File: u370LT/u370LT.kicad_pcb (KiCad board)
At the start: 2 copper layers, 1 part

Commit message: NB fixed up, SB started
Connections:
- U1 pad E16: unconnected-(U1-GTLREF-PadE16) -> Net-(U1-GTLREF-PadE16)
- U1 pad F17: unconnected-(U1-VTT-PadF17) -> Net-(U1-VTT-PadF17)
- U1 pad L4: Net-(U1-ST0) -> unconnected-(U1-ST0-PadL4)
- U1 pad M23: unconnected-(U1-GTLREF-PadM23) -> Net-(U1-GTLREF-PadE16)
- U1 pad M24: unconnected-(U1-VTT-PadM24) -> Net-(U1-VTT-PadF17)
- U1 pad M4: Net-(U1-ST0) -> unconnected-(U1-ST2-PadM4)

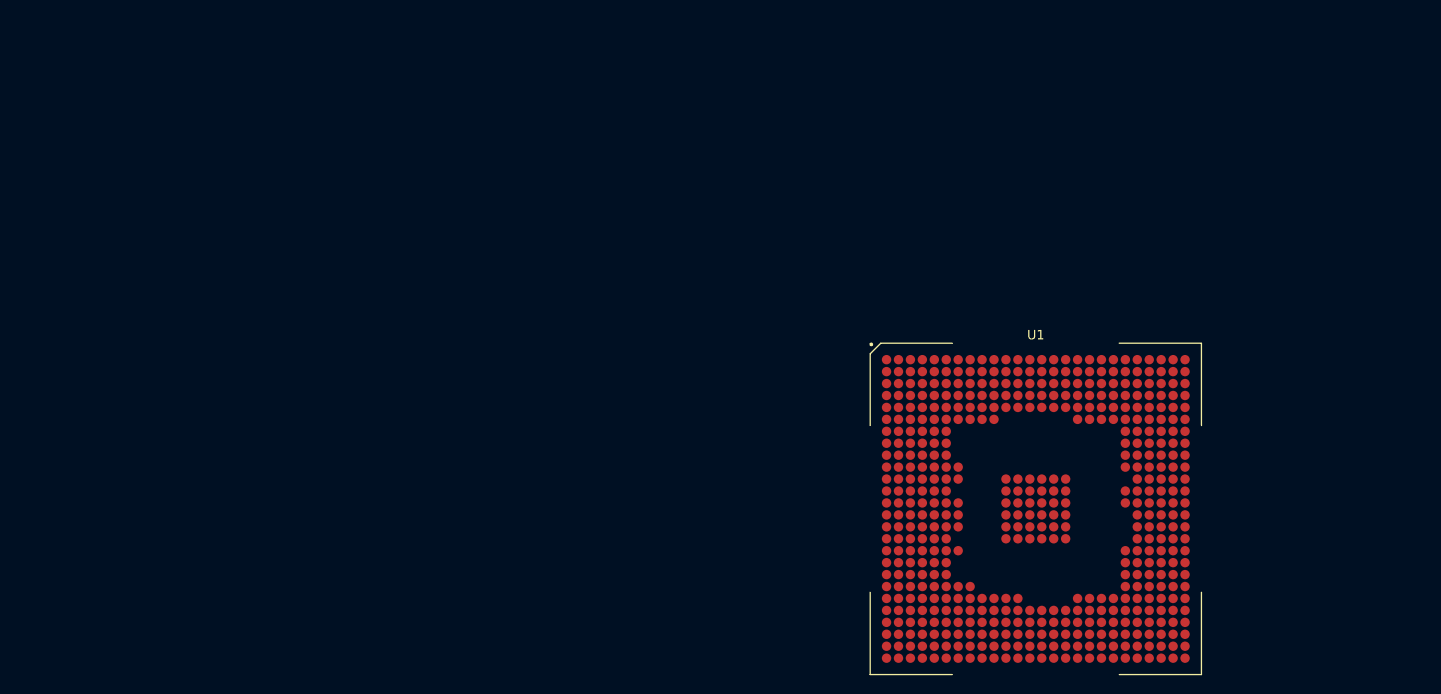
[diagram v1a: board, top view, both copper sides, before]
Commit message: Got NB/SB initially placed
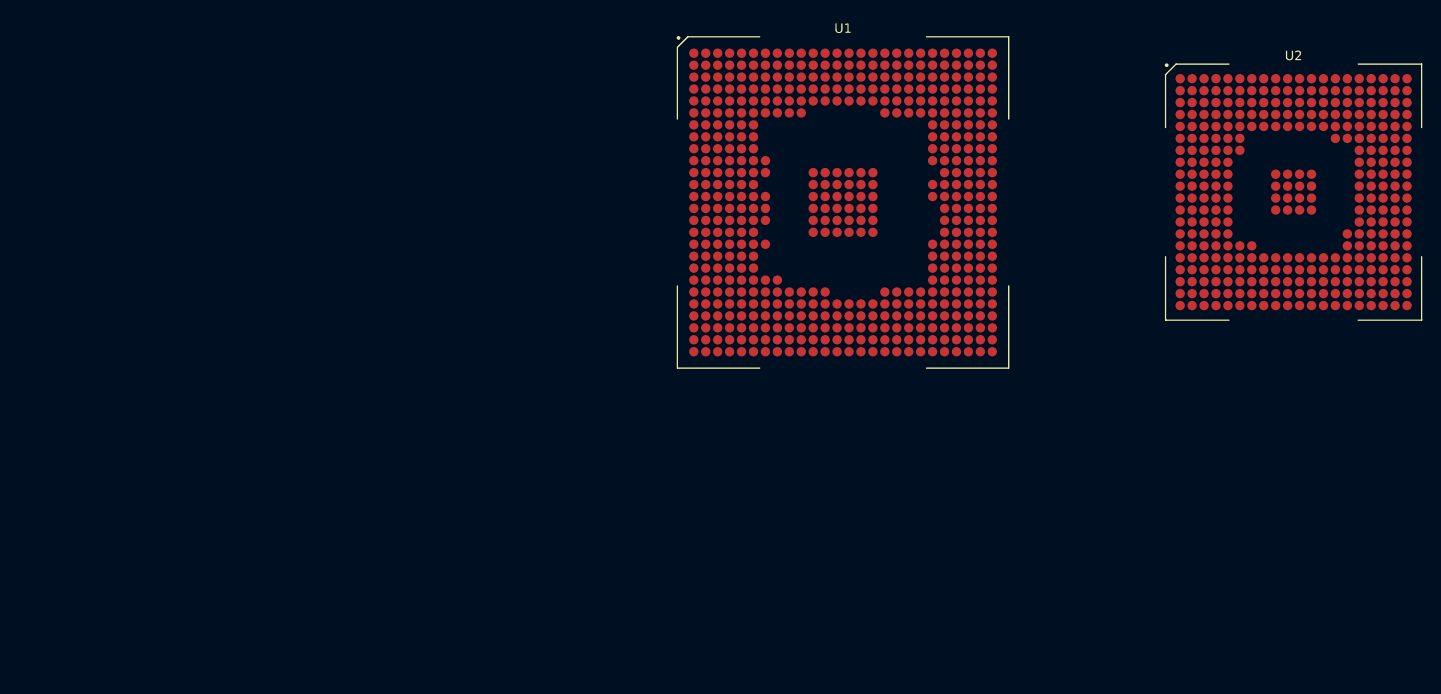
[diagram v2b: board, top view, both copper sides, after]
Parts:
- added U2: ~, Library:VT82C596B, F.Cu at (158.4, 47.0)
- U1: footprint Library:BGA-676_26x26_35.0x35.0mm -> Library:VT82C694X
- moved U1 38.5 mm to (110.5, 48.1)
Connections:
- U1 pad AF24: (no net) -> unconnected-(U1-CKE5-PadAF24)

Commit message: More 370 work
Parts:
- added U3: ~, Library:PGA370, F.Cu at (47.4, 51.2)
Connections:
- U1 pad A2: unconnected-(U1-AD20-PadA2) -> /North Bridge/AD20
- U1 pad A23: unconnected-(U1-HA29#-PadA23) -> HA29
- U1 pad A24: unconnected-(U1-HA24#-PadA24) -> HA24
- U1 pad A25: unconnected-(U1-HA22#-PadA25) -> HA22
- U1 pad A4: unconnected-(U1-AD25-PadA4) -> /North Bridge/AD25
- U1 pad A5: unconnected-(U1-AD29-PadA5) -> /North Bridge/AD29
- U1 pad B24: unconnected-(U1-HA27#-PadB24) -> HA27
- U1 pad B25: unconnected-(U1-HA20#-PadB25) -> HA20
- U1 pad B3: unconnected-(U1-AD22-PadB3) -> /North Bridge/AD22
- U1 pad B4: unconnected-(U1-AD27-PadB4) -> /North Bridge/AD27
- U1 pad B5: unconnected-(U1-AD28-PadB5) -> /North Bridge/AD28
- U1 pad C1: unconnected-(U1-AD19-PadC1) -> /North Bridge/AD19
- U1 pad C23: unconnected-(U1-HA26#-PadC23) -> HA26
- U1 pad C24: unconnected-(U1-HA28#-PadC24) -> HA28
- U1 pad C25: unconnected-(U1-HA23#-PadC25) -> HA23
- U1 pad C26: unconnected-(U1-HA21#-PadC26) -> HA21
- U1 pad C3: unconnected-(U1-AD21-PadC3) -> /North Bridge/AD21
- U1 pad C6: unconnected-(U1-AD31-PadC6) -> /North Bridge/AD31
- U1 pad D1: unconnected-(U1-AD16-PadD1) -> /North Bridge/AD16
- U1 pad D2: unconnected-(U1-AD18-PadD2) -> /North Bridge/AD18
- U1 pad D23: unconnected-(U1-HA31#-PadD23) -> HA31
- U1 pad D24: unconnected-(U1-HA25#-PadD24) -> HA25
- U1 pad D25: unconnected-(U1-HA18#-PadD25) -> HA18
- U1 pad D26: unconnected-(U1-HA19#-PadD26) -> HA19
- U1 pad D3: unconnected-(U1-AD17-PadD3) -> /North Bridge/AD17
- U1 pad D4: unconnected-(U1-AD23-PadD4) -> /North Bridge/AD23
- U1 pad D5: unconnected-(U1-AD26-PadD5) -> /North Bridge/AD26
- U1 pad E22: unconnected-(U1-HA30#-PadE22) -> HA30
- U1 pad E23: unconnected-(U1-HA15#-PadE23) -> HA15
- U1 pad E25: unconnected-(U1-HA17#-PadE25) -> HA17
- U1 pad E26: unconnected-(U1-HA16#-PadE26) -> HA16
- U1 pad E5: unconnected-(U1-AD24-PadE5) -> /North Bridge/AD24
- U1 pad E6: unconnected-(U1-AD30-PadE6) -> /North Bridge/AD30
- U1 pad F22: unconnected-(U1-HA11#-PadF22) -> HA11
- U1 pad F23: unconnected-(U1-HA12#-PadF23) -> HA12
- U1 pad F24: unconnected-(U1-HA13#-PadF24) -> HA13
- U1 pad F25: unconnected-(U1-HA14#-PadF25) -> HA14
- U1 pad F26: unconnected-(U1-HA08#-PadF26) -> HA8
- U1 pad G1: unconnected-(U1-AD13-PadG1) -> /North Bridge/AD13
- U1 pad G2: unconnected-(U1-AD14-PadG2) -> /North Bridge/AD14
- U1 pad G22: unconnected-(U1-HA10#-PadG22) -> HA10
- U1 pad G23: unconnected-(U1-HA5#-PadG23) -> HA5
- U1 pad G24: unconnected-(U1-HA7#-PadG24) -> HA7
- U1 pad G25: unconnected-(U1-HA3#-PadG25) -> HA3
- U1 pad G26: unconnected-(U1-HA9#-PadG26) -> HA9
- U1 pad G4: unconnected-(U1-AD15-PadG4) -> /North Bridge/AD15
- U1 pad H1: unconnected-(U1-AD8-PadH1) -> /North Bridge/AD8
- U1 pad H2: unconnected-(U1-AD7-PadH2) -> /North Bridge/AD7
- U1 pad H22: unconnected-(U1-HA4#-PadH22) -> HA4
- U1 pad H23: unconnected-(U1-HA6#-PadH23) -> HA6
- U1 pad H3: unconnected-(U1-AD10-PadH3) -> /North Bridge/AD10
- U1 pad H4: unconnected-(U1-AD12-PadH4) -> /North Bridge/AD12
- U1 pad H5: unconnected-(U1-AD11-PadH5) -> /North Bridge/AD11
- U1 pad J1: unconnected-(U1-AD5-PadJ1) -> /North Bridge/AD5
- U1 pad J2: unconnected-(U1-AD6-PadJ2) -> /North Bridge/AD6
- U1 pad J5: unconnected-(U1-AD9-PadJ5) -> /North Bridge/AD9
- U1 pad K2: unconnected-(U1-AD1-PadK2) -> /North Bridge/AD1
- U1 pad K3: unconnected-(U1-AD3-PadK3) -> /North Bridge/AD3
- U1 pad K4: unconnected-(U1-AD2-PadK4) -> /North Bridge/AD2
- U1 pad K5: unconnected-(U1-AD4-PadK5) -> /North Bridge/AD4
- U1 pad K6: unconnected-(U1-AD0-PadK6) -> /North Bridge/AD0
